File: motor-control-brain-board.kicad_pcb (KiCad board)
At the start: 4 copper layers, 60 x 50 mm, 107 parts, among them J1 GPIO, J10 PWM, J11 PWR, J12 POWER_SENSE, J13 MISC_SENSE, J2 I2C, J3 SERIAL_1, J4 SERIAL_2, J5 CAN, J6 SPI, J7 USB_C_Receptacle_USB2.0_16P, J8 SWD, J9 POS_SENSE, SW1 RST, U1 TLV76750QWDRBxQ1, U10 TLV6001DCK, U11 TLV6001DCK, U12 TLV6001DCK, U2 TLV76733QWDRBxQ1, U3 M95256-WMN6P, U4 STM32G474RETx, U5 TCAN1044V-Q1, U6 TLV6001DCK, U7 TLV6001DCK, U8 TLV6001DCK, U9 TLV6001DCK

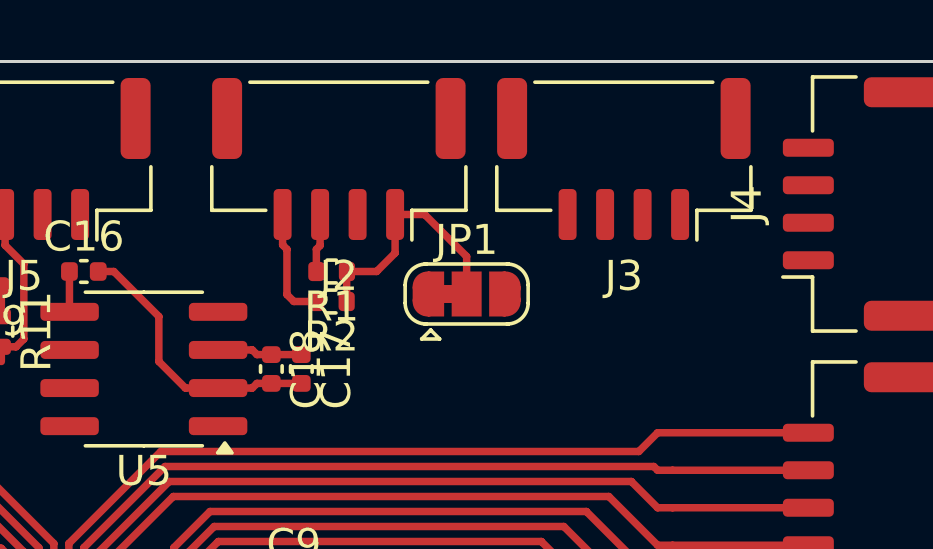
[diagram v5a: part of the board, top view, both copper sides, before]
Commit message: Changed +3V3 to +3v3A for thermistor supplies
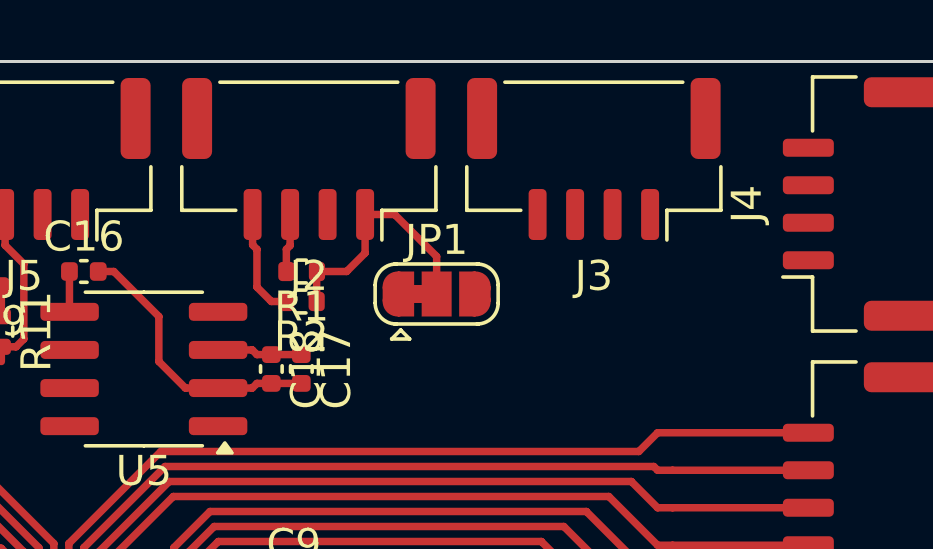
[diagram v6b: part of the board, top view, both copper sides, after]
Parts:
- moved J2 1.00 mm to (158.2, 73.2)
- moved J3 1.00 mm to (167.8, 73.2)
- moved JP1 1.00 mm to (162.5, 77.8)
- moved R1 1.00 mm to (158.0, 77.0)
- moved R2 1.00 mm to (158.0, 78.0)
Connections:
- R32 pad 2: +3.3V -> +3V3A
- R33 pad 2: +3.3V -> +3V3A

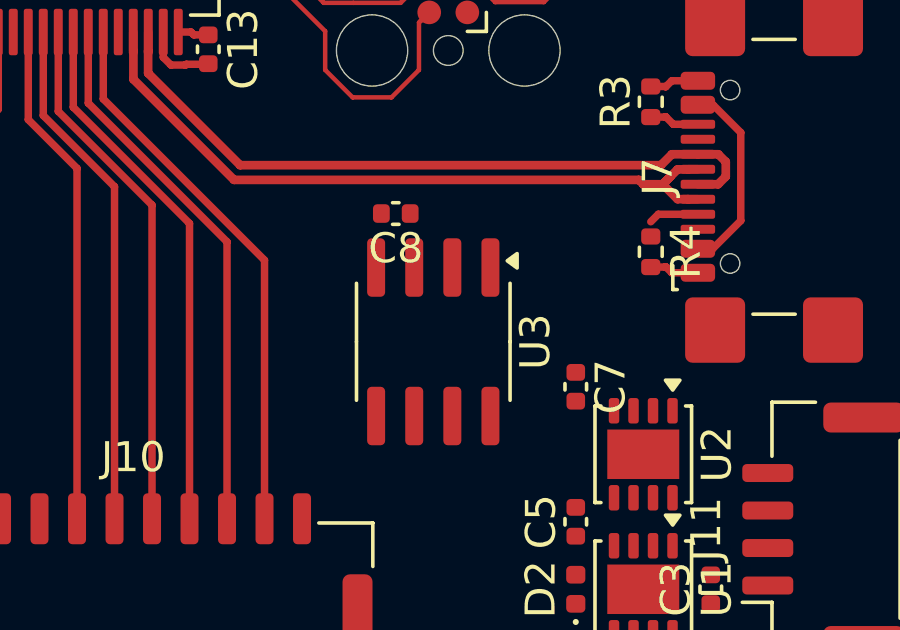
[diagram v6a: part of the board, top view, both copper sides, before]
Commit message: Changed EEPROM to TSSOT for smallness
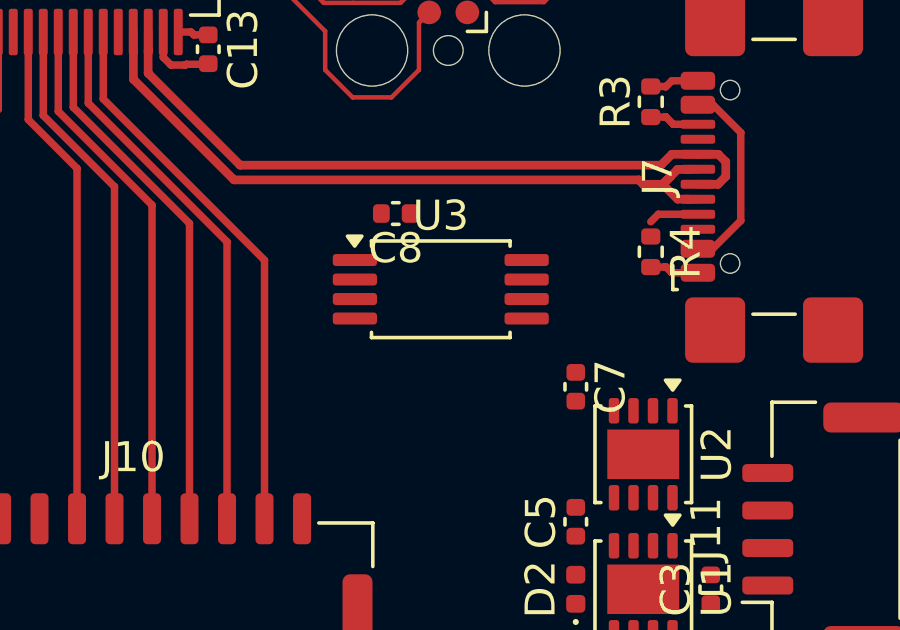
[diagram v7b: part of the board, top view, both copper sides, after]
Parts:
- U3: value M95256-WMN6P -> M95256-RDW6TP; footprint Package_SO:SOIC-8_3.9x4.9mm_P1.27mm -> Package_SO:TSSOP-8_4.4x3mm_P0.65mm
- moved U3 1.77 mm to (164.0, 107.2), turned to 0 degrees

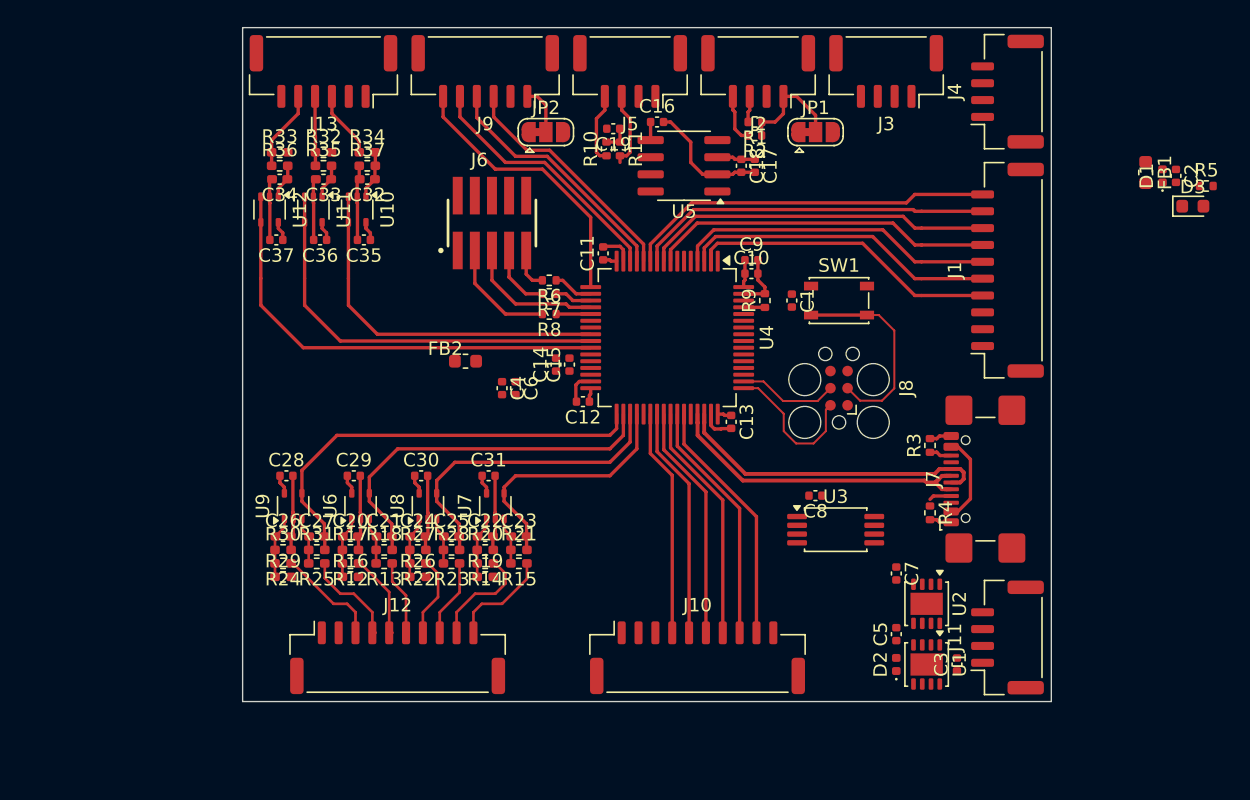
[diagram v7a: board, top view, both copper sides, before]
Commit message: Moved MCU to create room on top of board
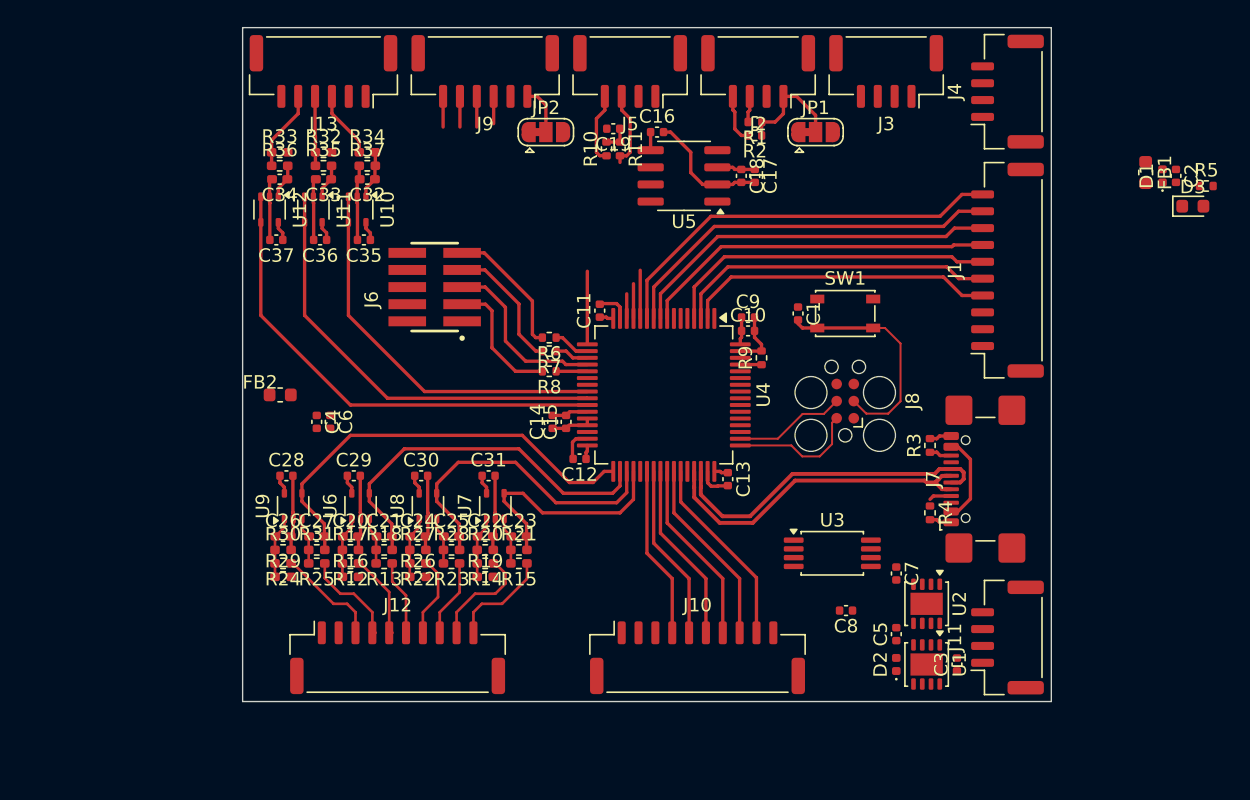
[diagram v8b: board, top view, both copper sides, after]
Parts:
- moved C4 14.0 mm to (125.5, 99.2)
- moved C6 14.0 mm to (126.5, 99.2)
- moved FB2 14.0 mm to (122.8, 97.2)
- moved C8 8.82 mm to (164.8, 113.2)
- moved J6 6.37 mm to (134.2, 89.2), turned to 90 degrees
- moved C10 4.26 mm to (157.5, 92.5)
- moved C11 4.26 mm to (146.5, 91.0)
- moved C12 4.26 mm to (145.0, 102.0)
- moved C13 4.26 mm to (156.0, 103.5)
- moved C14 4.26 mm to (143.0, 99.2)
- moved C15 4.26 mm to (144.0, 99.2)
- moved C9 4.26 mm to (157.5, 91.5)
- moved R9 4.26 mm to (158.5, 94.5)
- moved U4 4.26 mm to (151.2, 97.2)
- moved R6 4.25 mm to (142.8, 93.0)
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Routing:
- net /POS_C/RES_OUT: track 19.2 -> 4.10 mm
- net /POS_B: track 18.5 -> 4.85 mm
- net /POS_Z: track 20.7 -> 7.70 mm
- net /POS_A: track 17.8 -> 5.60 mm
- net /SPI_NSS: track 3.15 -> 10.0 mm
- net /SPI_SCK: track 4.98 -> 9.77 mm
- net /PWM_B_L: track 17.8 -> 13.7 mm
- net /PWM_B_H: track 17.5 -> 13.4 mm
- net /PWM_A_L: track 18.5 -> 14.3 mm
- net /PWM_C_L: track 17.2 -> 13.1 mm
- net /PWM_C_H: track 16.9 -> 12.8 mm
- net /PWM_A_H: track 18.1 -> 14.0 mm
- net +3V3A: track 10.1 -> 13.2 mm
- net /GPIO_7: track 27.4 -> 30.4 mm
- net /SPI_MISO: track 10.4 -> 13.1 mm
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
